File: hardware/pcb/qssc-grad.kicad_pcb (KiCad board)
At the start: 6 copper layers, 150 x 118 mm, 133 parts, among them J1 FT232RL, J10 USB-C, J12 BTB_HOST, J2 5V Barrel, J3 SMA, J4 12V LED, J7 RESET, J8 MW_GATE, J9 JTAG, U1 XC7A35T-1CSG324C, U3 ADF4351BCPZ, U5 GVA-84+, U8 W25Q128JVSIQ, Y1 100MHz XO

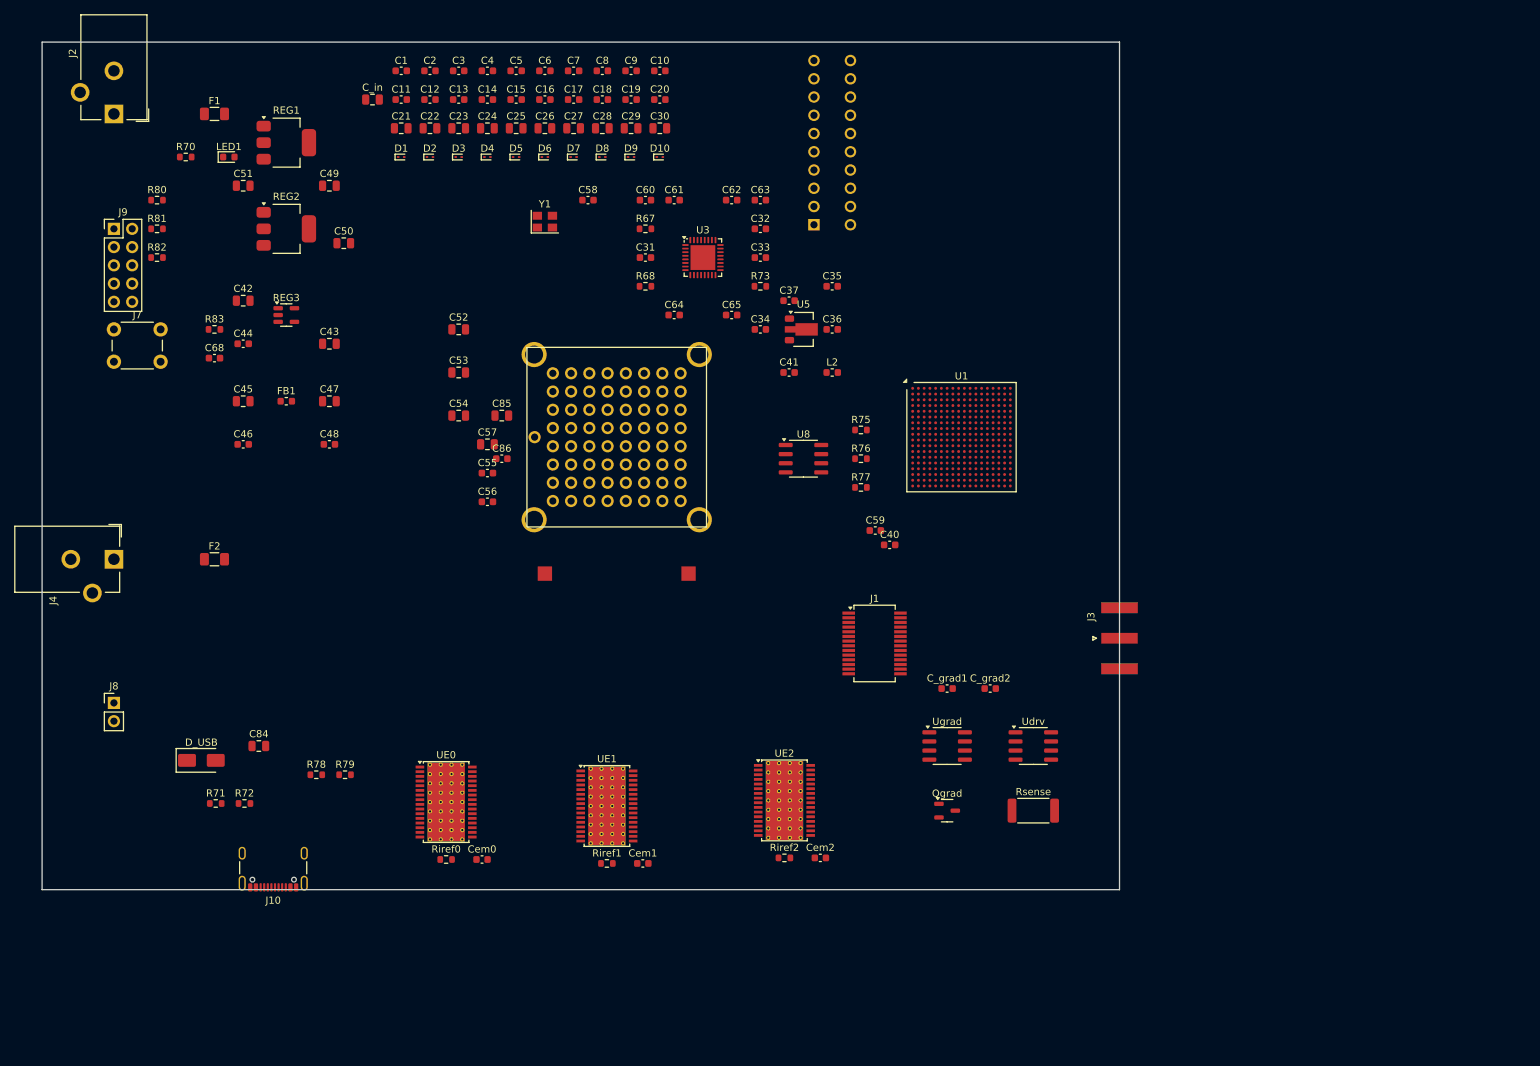
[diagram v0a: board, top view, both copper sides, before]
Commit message: pcb: route qssc-grad — 8 grad nets +5V feed, DRC 0/0/0
Fully routes the Invention-5 gradient variant on top of the injected main
board (1536 base tracks / 853 vias).  Final: 1964 tracks / 891 vias, DRC
0 errors / 0 unconnected / 0 footprint errors.

Pipeline (isolated worktree pcb/gradient-variant, main checkout untouched):
  sync_placement -> inject_base_routing -> copy_zones -> fill_zones
  then 3D A* maze router (maze_bridge_3d.py) for the 8 grad nets.

Routing per net:
  grad_cs/sclk/mosi  : BGA ball -> via-in-pad/dogbone -> In3/In4 -> Ugrad
  GRAD_COIL_N (2.2A) : Lgrad -> In3/In4 -> Qgrad drain (50.8mm, power w)
  GRAD_DAC_OUT/GATE/SENSE/NFB : In3/In4/B.Cu in the grad cluster
  +5V feed (Lgrad.1) : 5-pass maze chain to the +5V rail (73mm/3 vias)
  +5V grad cluster   : maze-chained Ugrad/Udrv/C_grad to the rail (124mm)
  grad_en            : 1-pad FPGA STATUS output, NC (intentionally unrouted)

Key fixes:
  - inject_base_routing: via layerset via CuStack() (microvias keep 2-layer
    set, was piercing In3/In4 -> 64 DRC shorts)
  - copy_zones: copy main's 2 zone outlines (route_qssc_pcb rebuild adds 297
    stitching vias that short injected signal tracks -> 150 violations)
  - maze_bridge_3d_pwr: fork allowing +5V (in PLANE_NETS) for the feed
  - grad_mosi via-in-pad at R1 south edge (121.2,59.6) clears SPI_CS In3
    (y=59.2) and T1; dogbone off-BGA blocked by grad_sclk + BGA column
  - swig proxy corruption (KiCad 10.x): capture netmap + pad index before
    any board.Remove(); fill zones in a fresh process (fill_zones.py)

Co-Authored-By: Claude Code <noreply@anthropic.com>
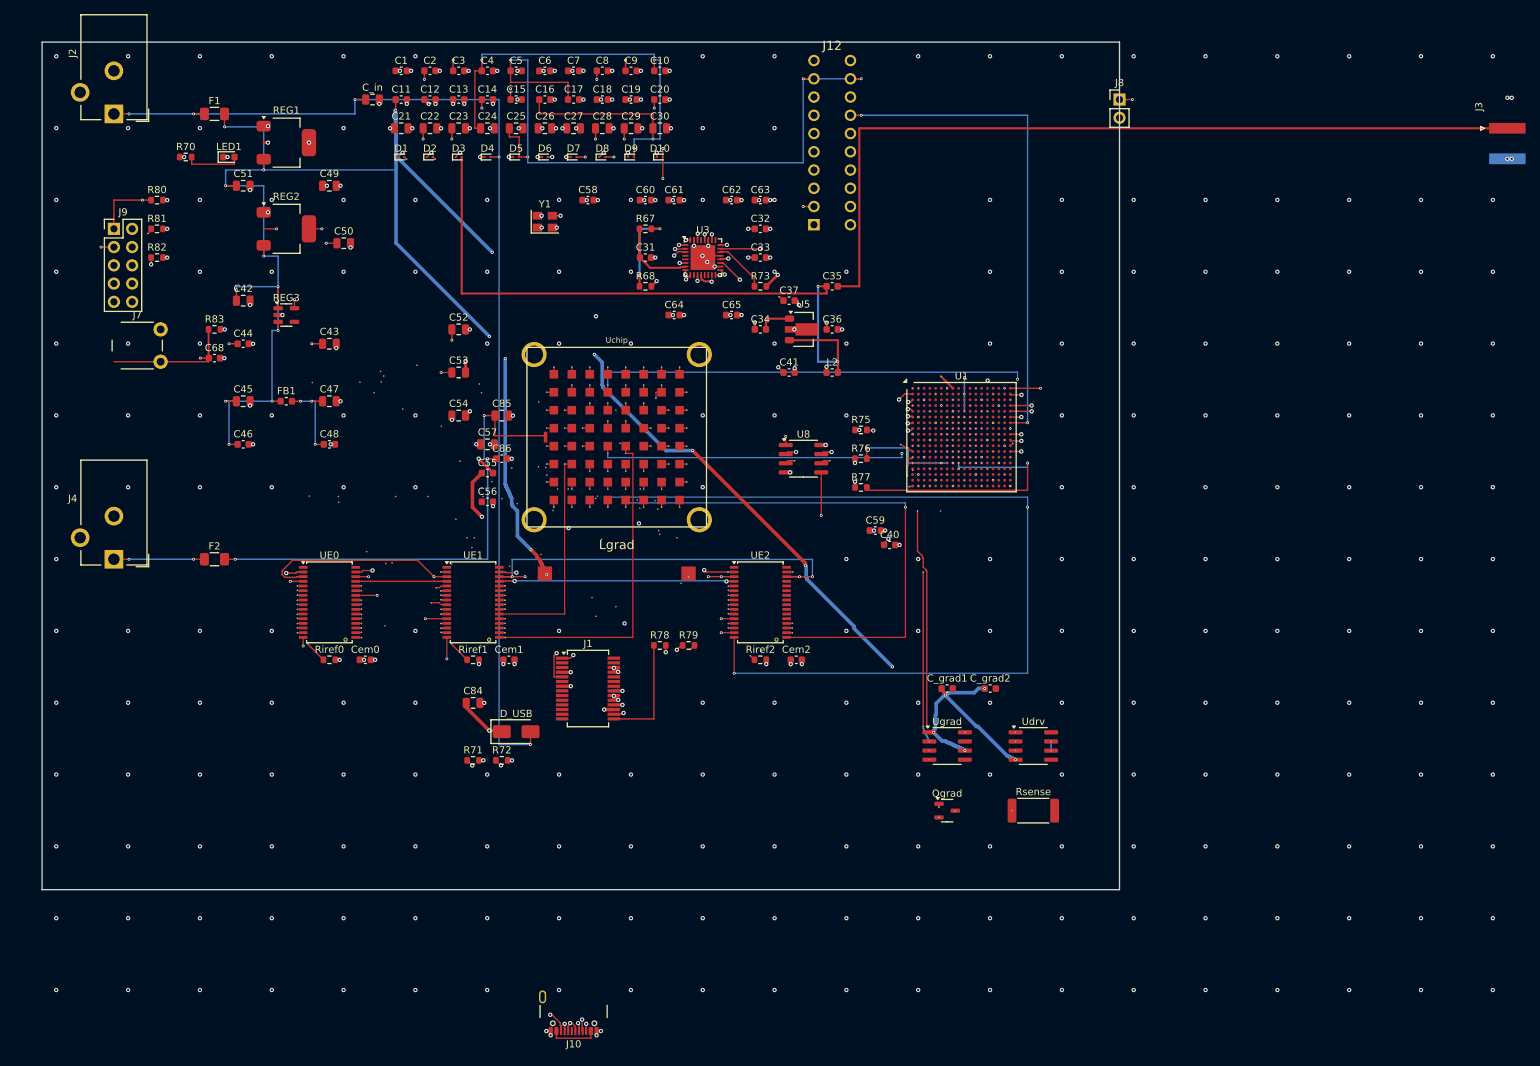
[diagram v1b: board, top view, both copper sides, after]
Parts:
- moved J8 163.3 mm to (150.0, 8.00)
- moved J3 89.2 mm to (204.0, 12.0)
- moved R78 51.1 mm to (86.0, 84.0)
- moved R79 51.1 mm to (90.0, 84.0)
- moved J10 46.4 mm to (74.0, 134.0)
- moved D_USB 44.0 mm to (66.0, 96.0)
- moved J1 40.4 mm to (76.0, 90.0)
- moved R71 36.3 mm to (60.0, 100.0)
- moved R72 36.3 mm to (64.0, 100.0)
- moved Cem1 33.9 mm to (65.0, 86.0)
- moved Riref1 33.9 mm to (60.0, 86.0)
- moved UE1 33.9 mm to (60.0, 78.0)
- moved Cem0 32.2 mm to (45.0, 86.0)
- moved Riref0 32.2 mm to (40.0, 86.0)
- moved UE0 32.2 mm to (40.0, 78.0)
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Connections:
- U3 pad : GND -> (no net)
- UE0 pad : GND -> (no net)
- UE1 pad : GND -> (no net)
- UE2 pad : GND -> (no net)
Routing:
- net +5V: track 0.00 -> 468.5 mm, vias 0 -> 29
- net +1V0: track 0.00 -> 255.6 mm, vias 0 -> 26
- net +1V8: track 0.00 -> 221.6 mm, vias 0 -> 16
- net emitter_cat11: track 0.00 -> 198.6 mm, vias 0 -> 3
- net +5V_RF: track 0.00 -> 189.9 mm, vias 0 -> 8
- net USB_DP: track 0.00 -> 183.6 mm, vias 0 -> 3
- net +5V_IN: track 0.00 -> 155.8 mm, vias 0 -> 5
- net TCK: track 0.00 -> 153.4 mm, vias 0 -> 3
- net mw_gate: track 0.00 -> 151.8 mm, vias 0 -> 4
- net USB_DM: track 0.00 -> 150.7 mm, vias 0 -> 4
- net emitter_cat35: track 0.00 -> 147.7 mm, vias 0 -> 3
- net TDO: track 0.00 -> 147.3 mm, vias 0 -> 2
- net emitter_cat59: track 0.00 -> 131.2 mm, vias 0 -> 3
- net reset: track 0.00 -> 128.3 mm, vias 0 -> 2
- net em_xlat: track 0.00 -> 116.6 mm, vias 0 -> 6
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- added copper zone on In2.Cu, net +3V3
- added copper zone on In1.Cu, net GND

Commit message: pcb: qssc-grad net-tie coil + Rgrad_feed + V-row grad pins — DRC 0/0/0
Fixes the Invention-5 gradient coil blockers found in the variant review:

1. Coil is now a real KiCad net-tie footprint (net_tie_pad_groups "1, 2")
   with a filled fp_poly on F.Cu -- the coil trace CONDUCTS (was F.Fab =
   open circuit).  A 0R feed resistor Rgrad_feed bridges +5V -> GRAD_COIL_P
   -> Lgrad pad1, so the +5V plane and GRAD_COIL_N stay separate everywhere
   except at the resistor: the MOSFET drain cannot bypass the coil via the
   +5V plane.  Lgrad pad1 = GRAD_COIL_P, pad2 = GRAD_COIL_N.

2. grad FPGA pins moved to the south edge (V6/V9/V12/V7) in xdc + ballmap +
   generator net map -- the old M1/N1/R1/T1 pins conflicted with base-board
   inner-layer escapes.  grad_sclk (V9) gets a pre-placed dogbone fanout via
   (add_grad_fanout) so the 3D maze router can escape the BGA.

3. maze_bridge_3d.py de-forked: --keep-power[=NET,..] flag replaces the
   separate maze_bridge_3d_pwr.py (deleted).  Routes all 10 grad nets + the
   +5V feed across B.Cu/In3/In4/F.Cu with via transitions.

4. Generator min_hole_to_hole 0.25 -> 0.20 to match the hand-routed main
   board (whose dense 0.10mm-drill HDI vias were DRC'd at 0.20); the old
   0.25 tripped 3 hole_near_hole errors on re-injected emitter_cat vias.

5. Deleted stale tools: fix_uchip_pads.py (wrong premise -- main board uses
   the 1.7mm PTH female-header socket, not 1.2mm SMD ACF) + maze_bridge_3d_pwr.py
   + tracked chip_module.closed.* scratch boards.

Result: qssc-grad 2448 tracks / 817 vias, DRC 0 errors / 0 unconnected / 0
footprint errors, ERC 0.  Base qssc.*/chip_module.* boards byte-unchanged.

Co-Authored-By: Claude Code <noreply@anthropic.com>
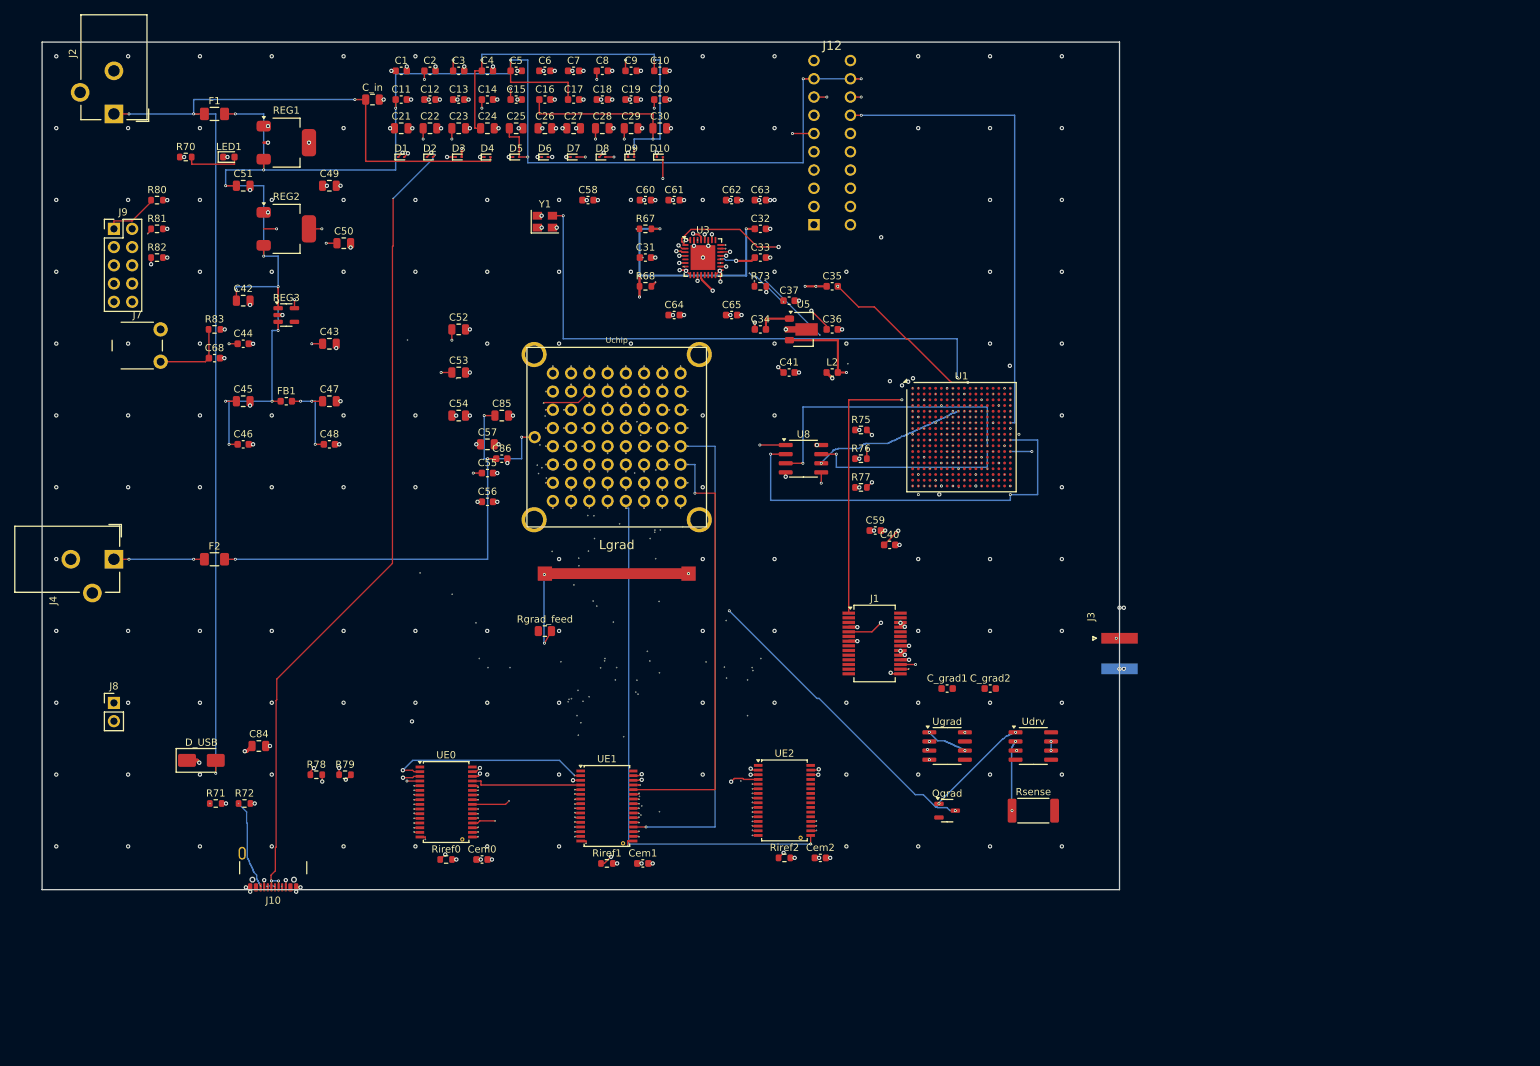
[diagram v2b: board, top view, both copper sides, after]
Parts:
- added Rgrad_feed: 0R, R_0805_2012Metric, F.Cu at (70.0, 82.0)
- moved J8 163.3 mm to (10.0, 92.0)
- moved J3 89.2 mm to (150.0, 83.0)
- moved R78 51.1 mm to (38.2, 102.0)
- moved R79 51.1 mm to (42.2, 102.0)
- moved J10 46.4 mm to (32.2, 114.0)
- moved D_USB 44.0 mm to (22.2, 100.0)
- moved J1 40.4 mm to (115.9, 83.7)
- moved R71 36.3 mm to (24.2, 106.0)
- moved R72 36.3 mm to (28.2, 106.0)
- moved Cem1 33.9 mm to (83.6, 114.3)
- moved Riref1 33.9 mm to (78.6, 114.3)
- moved UE1 33.9 mm to (78.6, 106.3)
- moved Cem0 32.2 mm to (61.2, 113.8)
- moved Riref0 32.2 mm to (56.2, 113.8)
- moved UE0 32.2 mm to (56.2, 105.8)
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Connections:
- Lgrad pad 1: +5V -> GRAD_COIL_P
- U1 pad M1: grad_cs -> (no net)
- U1 pad N1: grad_sclk -> (no net)
- U1 pad R1: grad_mosi -> (no net)
- U1 pad T1: grad_en -> (no net)
- U1 pad V12: (no net) -> grad_mosi
- U1 pad V6: (no net) -> grad_cs
- U1 pad V7: (no net) -> grad_en
- U1 pad V9: (no net) -> grad_sclk
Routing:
- net +5V: track 468.5 -> 247.0 mm, vias 29 -> 17
- net TMS: track 8.40 -> 138.4 mm, vias 1 -> 3
- net TDI: track 7.31 -> 134.5 mm, vias 1 -> 3
- net emitter_cat11: track 198.6 -> 78.3 mm
- net emitter_cat35: track 147.7 -> 58.8 mm
- net clk_100mhz: track 1.13 -> 81.8 mm, vias 1 -> 3
- net USB_DP_F: track 15.8 -> 90.5 mm, vias 0 -> 2
- net emitter_cat59: track 131.2 -> 57.8 mm, vias 3 -> 4
- net USB_DM_F: track 16.0 -> 87.2 mm, vias 2 -> 3
- net USB_DM: track 150.7 -> 208.2 mm, vias 4 -> 5
- net mw_gate: track 151.8 -> 203.2 mm, vias 4 -> 2
- net refclk_25m: track 2.35 -> 53.7 mm, vias 1 -> 3
- net J3_SIG: track 115.2 -> 68.2 mm, vias 0 -> 3
- net 3V3OUT: track 45.1 -> 91.5 mm
- net +5V_RF: track 189.9 -> 148.0 mm
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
